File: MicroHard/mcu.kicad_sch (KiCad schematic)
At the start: 1 part, among them U3 efm32gg842f1024

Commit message: MCU schematic
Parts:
- removed U3: efm32gg842f1024, EFM32GG842F1024:QFP64_10X10, symbol EFM32GG842F1024:efm32gg842f1024
- added C45, C50, C54: 10 µ, symbol Device:C_Polarized_US
- added C46, C48, C49, C52: 0.1 µ, symbol Device:C
- added C47: 1 µ, symbol Device:C
- added C51, C53: 10 n, symbol Device:C
- added C55, C56: 12 p, symbol Device:C
- added D1: LED, symbol Device:LED
- added J1: MCU_Debug, Connector_PinHeader_1.00mm:PinHeader_2x10_P1.00mm_Vertical, symbol Connector_Generic:Conn_02x10_Odd_Even
- added J2: Controller Connector, symbol Connector:Conn_01x07_Socket
- added J3: GPIO_header, Connector_JST:JST_XH_B8B-XH-AM_1x08_P2.50mm_Vertical, symbol Connector:Conn_01x08_Pin
- added R11: R, symbol Device:R
- added R12, R13: 10k, Resistor_SMD:R_1206_3216Metric_Pad1.30x1.75mm_HandSolder, symbol Device:R
- added SW1, SW2: KMR221NGLFS, KMR221_CNK, symbol Button:KMR221NGLFS
- added U3: EFM32GG842F1024, EFM32GG842F1024:QFP64_10X10, symbol EFM32GG842F1024:efm32gg842f1024_improved_layout
- added Y1: 48 MHz, symbol Device:Crystal_GND24
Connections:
- new net: J3.1 (Pin_1), U3.13 (PC4)
- new net: J3.2 (Pin_2), U3.14 (PC5)
- new net: C56.1, U3.24 (PB13), Y1.3
- new net: C55.1, U3.25 (PB14), Y1.1
- new net: J3.3 (Pin_3), U3.37 (PC6)
- new net: J3.4 (Pin_4), U3.38 (PC7)
- new net: J3.5 (Pin_5), U3.45 (PC12)
- new net: J3.6 (Pin_6), U3.46 (PC13)
- new net: J3.7 (Pin_7), U3.47 (PC14)
- new net: J3.8 (Pin_8), U3.48 (PC15)
- new net: J1.9 (Pin_9), U3.49 (PF0)
- new net: J1.7 (Pin_7), U3.50 (PF1)
- new net: J1.13 (Pin_13), U3.51 (PF2)
- new net: R11.2, U3.9 (PB3)
- new net: R12.1, SW1.2
- new net: D1.2 (A), R11.1
- new net: C47.1, U3.40 (DECOUPLE)
- new net: R13.2, SW2.1
- new net +3.3V: C45.1, C46.1, C48.1, C49.1, C50.1, C51.1, C52.1, C53.1, C54.1, J1.1 (Pin_1), R13.1, SW1.1, U3.23 (AVDD_1), U3.26 (IOVDD_3), U3.27 (AVDD_0), U3.39 (VDD_DREG), U3.55 (IOVDD_5), U3.7 (IOVDD_0)
- new net +3.3VA: J2.1 (Pin_1)
- new net Btn_1: SW1.3, U3.10 (PB4)
- new net ControllerBtn: J2.6 (Pin_6), U3.31 (PD3)
- new net ControllerX: J2.3 (Pin_3), U3.28 (PD0)
- new net ControllerY: J2.4 (Pin_4), U3.29 (PD1)
- new net ControllerZ: J2.5 (Pin_5), U3.30 (PD2)
- new net FPGA_GPIO0: U3.58 (PE9)
- new net FPGA_GPIO1: U3.57 (PE8)
- new net FPGA_RESET: U3.44 (PE7)
- new net FPGA_US0_CLK: U3.61 (PE12)
- new net FPGA_US0_CS: U3.62 (PE13)
- new net FPGA_US0_RX: U3.60 (PE11)
- new net FPGA_US0_TX: U3.59 (PE10)
- new net GND: C45.2, C46.2, C47.2, C48.2, C49.2, C50.2, C51.2, C52.2, C53.2, C54.2, C55.2, C56.2, D1.1 (K), J1.10 (Pin_10), J1.12 (Pin_12), J1.14 (Pin_14), J1.16 (Pin_16), J1.18 (Pin_18), J1.20 (Pin_20), J1.4 (Pin_4), J1.6 (Pin_6), J1.8 (Pin_8), J2.2 (Pin_2), R12.2, SW2.2, U3.22 (VSS), U3.56 (VSS), U3.8 (VSS), Y1.2, Y1.4
- new net I2C0_SCL: U3.2 (PA1)
- new net I2C0_SDA: U3.1 (PA0)
- new net MCU_Reset: J1.15 (Pin_15), SW2.4, U3.20 (RESETN)
- no-connect marks 0 -> 9
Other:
- title: (none) -> Microcontroller unit

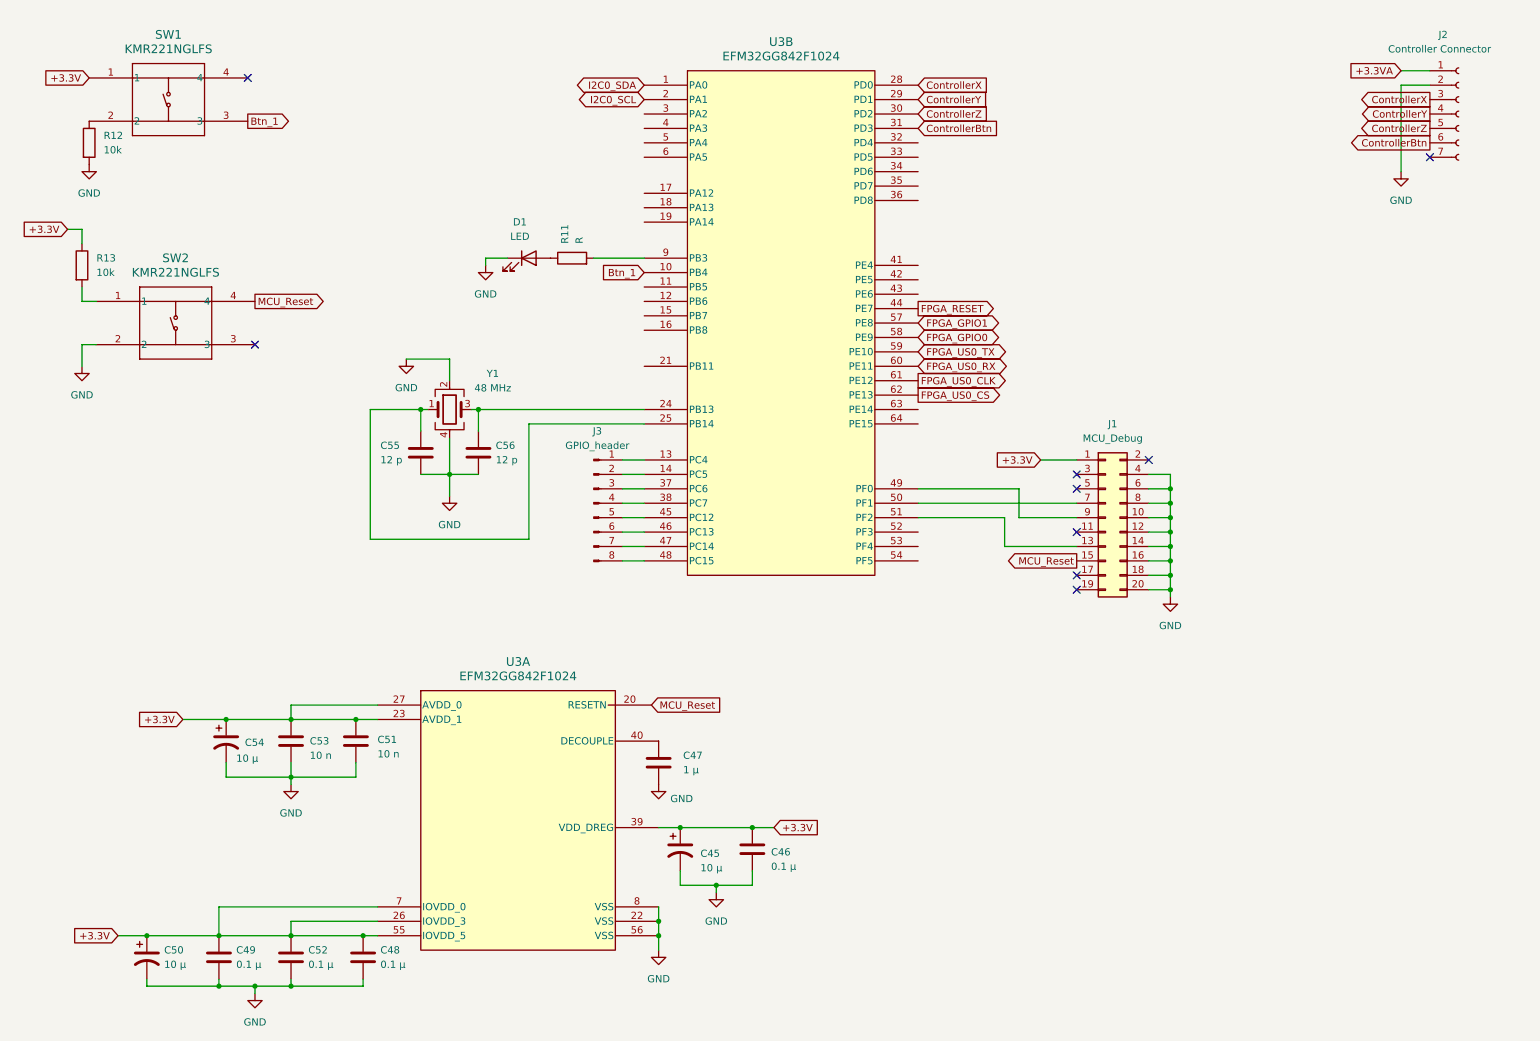
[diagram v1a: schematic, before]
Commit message: feat: VGA out lines from FPGA drawn
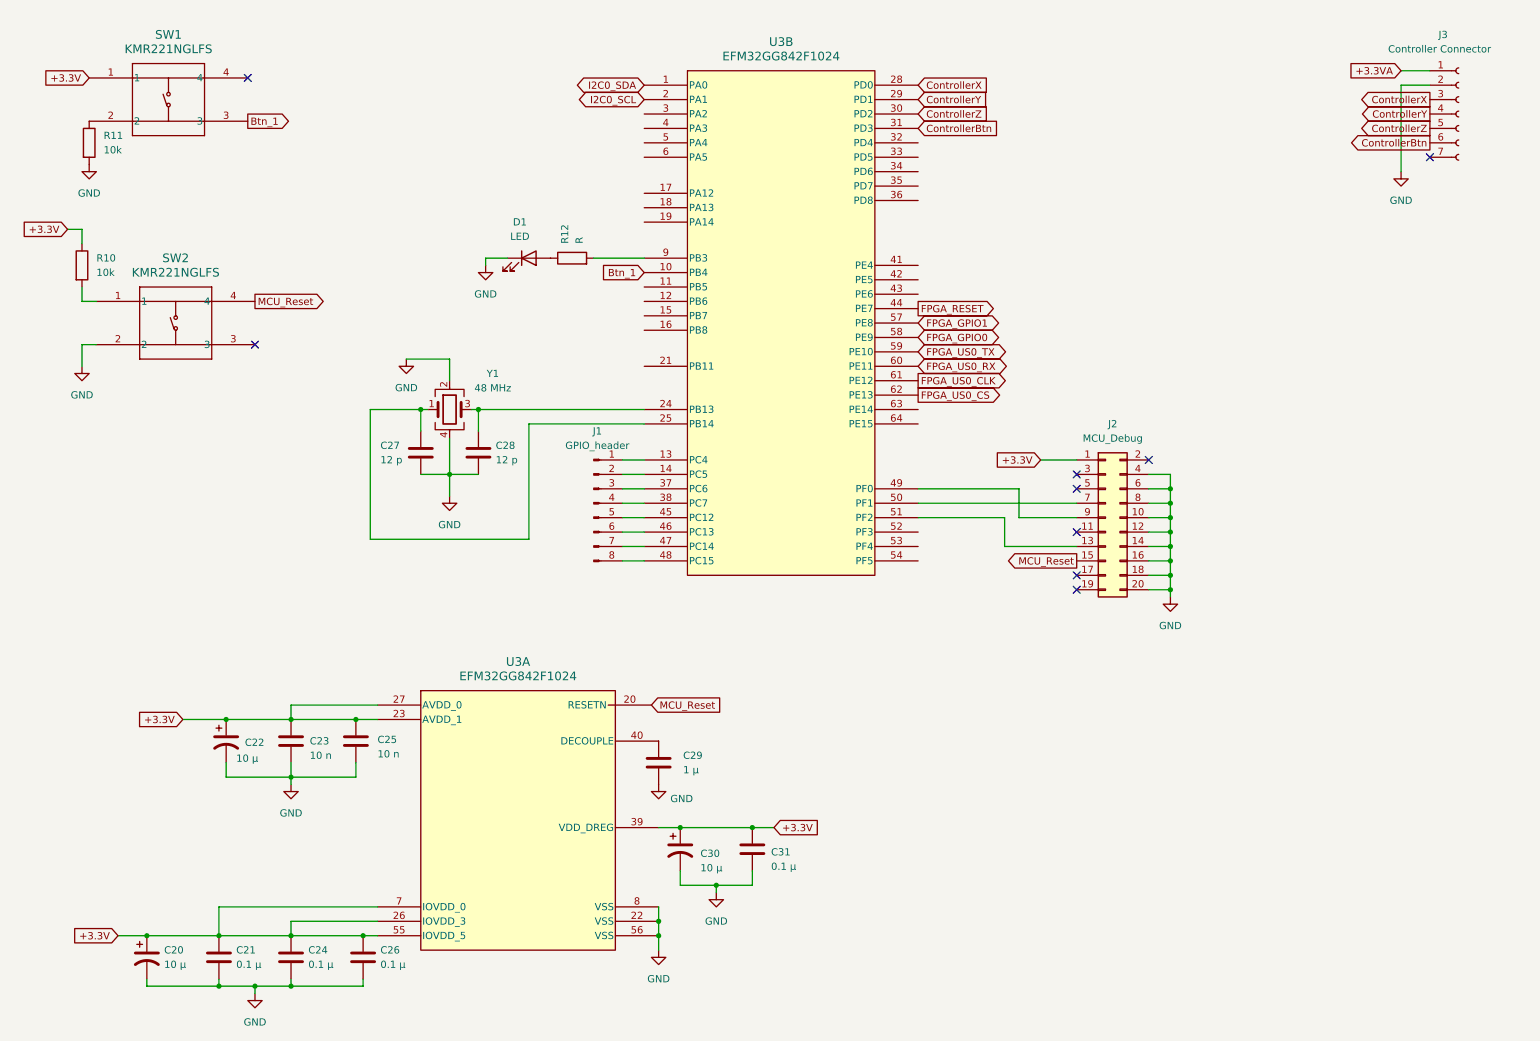
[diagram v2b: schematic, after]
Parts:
- renumbered C50 to C20, C49 to C21, C54 to C22, C53 to C23, C52 to C24, C51 to C25, C48 to C26, C55 to C27, C56 to C28, C47 to C29, C45 to C30, C46 to C31, J3 to J1, J1 to J2, J2 to J3, R13 to R10, R12 to R11, R11 to R12
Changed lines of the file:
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@@
 		(on_board yes)
 		(dnp no)
-		(property "Reference" "C46"
+		(property "Reference" "C31"
 			(at 149.352 164.338 0)
 			(effects
@@
 			(project ""
 				(path "/578bd531-a491-4b15-a479-460d159ffc14/51bb8540-90e7-4b9a-973c-776e3825d084"
-					(reference "C46")
+					(reference "C31")
 					(unit 1)
 				)
@@
 		(on_board yes)
 		(dnp no)
-		(property "Reference" "C52"
+		(property "Reference" "C24"
 			(at 67.818 181.61 0)
 			(effects
@@
 			(project ""
 				(path "/578bd531-a491-4b15-a479-460d159ffc14/51bb8540-90e7-4b9a-973c-776e3825d084"
-					(reference "C52")
+					(reference "C24")
 					(unit 1)
 				)
@@
 		(on_board yes)
 		(dnp no)
-		(property "Reference" "#PWR020"
+		(property "Reference" "#PWR016"
 			(at 129.54 158.75 0)
 			(effects
@@
 			(project ""
 				(path "/578bd531-a491-4b15-a479-460d159ffc14/51bb8540-90e7-4b9a-973c-776e3825d084"
-					(reference "#PWR020")
+					(reference "#PWR016")
 					(unit 1)
 				)
@@
 		(dnp no)
 		(fields_autoplaced yes)
-		(property "Reference" "R12"
+		(property "Reference" "R11"
 			(at 31.75 38.0999 0)
 			(effects
@@
 			(project ""
 				(path "/578bd531-a491-4b15-a479-460d159ffc14/51bb8540-90e7-4b9a-973c-776e3825d084"
-					(reference "R12")
+					(reference "R11")
 					(unit 1)
 				)
@@
 		(dnp no)
 		(fields_autoplaced yes)
-		(property "Reference" "R11"
+		(property "Reference" "R12"
 			(at 113.0299 57.15 0)
 			(effects
@@
 			(project ""
 				(path "/578bd531-a491-4b15-a479-460d159ffc14/51bb8540-90e7-4b9a-973c-776e3825d084"
-					(reference "R11")
+					(reference "R12")
 					(unit 1)
 				)
@@
 		(dnp no)
 		(fields_autoplaced yes)
-		(property "Reference" "#PWR025"
+		(property "Reference" "#PWR013"
 			(at 85.09 83.82 0)
 			(effects
@@
 			(project ""
 				(path "/578bd531-a491-4b15-a479-460d159ffc14/51bb8540-90e7-4b9a-973c-776e3825d084"
-					(reference "#PWR025")
+					(reference "#PWR013")
 					(unit 1)
 				)
@@
 		(on_board yes)
 		(dnp no)
-		(property "Reference" "C53"
+		(property "Reference" "C23"
 			(at 68.072 144.78 0)
 			(effects
@@
 			(project ""
 				(path "/578bd531-a491-4b15-a479-460d159ffc14/51bb8540-90e7-4b9a-973c-776e3825d084"
-					(reference "C53")
+					(reference "C23")
 					(unit 1)
 				)
@@
 		(on_board yes)
 		(dnp no)
-		(property "Reference" "C49"
+		(property "Reference" "C21"
 			(at 55.118 181.61 0)
 			(effects
@@
 			(project ""
 				(path "/578bd531-a491-4b15-a479-460d159ffc14/51bb8540-90e7-4b9a-973c-776e3825d084"
-					(reference "C49")
+					(reference "C21")
 					(unit 1)
 				)
@@
 		(dnp no)
 		(fields_autoplaced yes)
-		(property "Reference" "#PWR027"
+		(property "Reference" "#PWR09"
 			(at 27.94 85.09 0)
 			(effects
@@
 			(project ""
 				(path "/578bd531-a491-4b15-a479-460d159ffc14/51bb8540-90e7-4b9a-973c-776e3825d084"
-					(reference "#PWR027")
+					(reference "#PWR09")
 					(unit 1)
 				)
@@
 		(dnp no)
 		(fields_autoplaced yes)
-		(property "Reference" "#PWR015"
+		(property "Reference" "#PWR020"
 			(at 260.35 50.8 0)
 			(effects
@@
 			(project ""
 				(path "/578bd531-a491-4b15-a479-460d159ffc14/51bb8540-90e7-4b9a-973c-776e3825d084"
-					(reference "#PWR015")
+					(reference "#PWR020")
 					(unit 1)
 				)
@@
 		(on_board yes)
 		(dnp no)
-		(property "Reference" "J2"
+		(property "Reference" "J3"
 			(at 266.954 20.32 0)
 			(effects
@@
 			(project ""
 				(path "/578bd531-a491-4b15-a479-460d159ffc14/51bb8540-90e7-4b9a-973c-776e3825d084"
-					(reference "J2")
+					(reference "J3")
 					(unit 1)
 				)
@@
 		(dnp no)
 		(fields_autoplaced yes)
-		(property "Reference" "J3"
+		(property "Reference" "J1"
 			(at 118.745 90.17 0)
 			(effects
@@
 			(project ""
 				(path "/578bd531-a491-4b15-a479-460d159ffc14/51bb8540-90e7-4b9a-973c-776e3825d084"
-					(reference "J3")
+					(reference "J1")
 					(unit 1)
 				)
@@
 		(on_board yes)
 		(dnp no)
-		(property "Reference" "C50"
+		(property "Reference" "C20"
 			(at 42.418 181.61 0)
 			(effects
@@
 			(project "MicroHard"
 				(path "/578bd531-a491-4b15-a479-460d159ffc14/51bb8540-90e7-4b9a-973c-776e3825d084"
-					(reference "C50")
+					(reference "C20")
 					(unit 1)
 				)
@@
 		(on_board yes)
 		(dnp no)
-		(property "Reference" "C56"
+		(property "Reference" "C28"
 			(at 100.838 92.71 0)
 			(effects
@@
 			(project ""
 				(path "/578bd531-a491-4b15-a479-460d159ffc14/51bb8540-90e7-4b9a-973c-776e3825d084"
-					(reference "C56")
+					(reference "C28")
 					(unit 1)
 				)
@@
 		(dnp no)
 		(fields_autoplaced yes)
-		(property "Reference" "#PWR016"
+		(property "Reference" "#PWR012"
 			(at 64.77 158.75 0)
 			(effects
@@
 			(project ""
 				(path "/578bd531-a491-4b15-a479-460d159ffc14/51bb8540-90e7-4b9a-973c-776e3825d084"
-					(reference "#PWR016")
+					(reference "#PWR012")
 					(unit 1)
 				)
@@
 		(dnp no)
 		(fields_autoplaced yes)
-		(property "Reference" "#PWR024"
+		(property "Reference" "#PWR014"
 			(at 92.71 107.95 0)
 			(effects
@@
 			(project ""
 				(path "/578bd531-a491-4b15-a479-460d159ffc14/51bb8540-90e7-4b9a-973c-776e3825d084"
-					(reference "#PWR024")
+					(reference "#PWR014")
 					(unit 1)
 				)
@@
 		(dnp no)
 		(fields_autoplaced yes)
-		(property "Reference" "#PWR014"
+		(property "Reference" "#PWR018"
 			(at 139.7 177.8 0)
 			(effects
@@
 			(project ""
 				(path "/578bd531-a491-4b15-a479-460d159ffc14/51bb8540-90e7-4b9a-973c-776e3825d084"
-					(reference "#PWR014")
+					(reference "#PWR018")
 					(unit 1)
 				)
@@
 		(on_board yes)
 		(dnp no)
-		(property "Reference" "C51"
+		(property "Reference" "C25"
 			(at 80.01 144.526 0)
 			(effects
@@
 			(project ""
 				(path "/578bd531-a491-4b15-a479-460d159ffc14/51bb8540-90e7-4b9a-973c-776e3825d084"
-					(reference "C51")
+					(reference "C25")
 					(unit 1)
 				)
@@
 		(on_board yes)
 		(dnp no)
-		(property "Reference" "C48"
+		(property "Reference" "C26"
 			(at 80.518 181.61 0)
 			(effects
@@
 			(project ""
 				(path "/578bd531-a491-4b15-a479-460d159ffc14/51bb8540-90e7-4b9a-973c-776e3825d084"
-					(reference "C48")
+					(reference "C26")
 					(unit 1)
 				)
@@
 		(dnp no)
 		(fields_autoplaced yes)
-		(property "Reference" "J1"
+		(property "Reference" "J2"
 			(at 209.55 88.9 0)
 			(effects
@@
 			(project ""
 				(path "/578bd531-a491-4b15-a479-460d159ffc14/51bb8540-90e7-4b9a-973c-776e3825d084"
-					(reference "J1")
+					(reference "J2")
 					(unit 1)
 				)
@@
 		(on_board yes)
 		(dnp no)
-		(property "Reference" "C54"
+		(property "Reference" "C22"
 			(at 56.642 145.034 0)
 			(effects
@@
 			(project ""
 				(path "/578bd531-a491-4b15-a479-460d159ffc14/51bb8540-90e7-4b9a-973c-776e3825d084"
-					(reference "C54")
+					(reference "C22")
 					(unit 1)
 				)
@@
 		(on_board yes)
 		(dnp no)
-		(property "Reference" "C45"
+		(property "Reference" "C30"
 			(at 136.906 164.592 0)
 			(effects
@@
 			(project "MicroHard"
 				(path "/578bd531-a491-4b15-a479-460d159ffc14/51bb8540-90e7-4b9a-973c-776e3825d084"
-					(reference "C45")
+					(reference "C30")
 					(unit 1)
 				)
@@
 		(dnp no)
 		(fields_autoplaced yes)
-		(property "Reference" "#PWR022"
+		(property "Reference" "#PWR015"
 			(at 99.06 67.31 0)
 			(effects
@@
 			(project ""
 				(path "/578bd531-a491-4b15-a479-460d159ffc14/51bb8540-90e7-4b9a-973c-776e3825d084"
-					(reference "#PWR022")
+					(reference "#PWR015")
 					(unit 1)
 				)
@@
 		(dnp no)
 		(fields_autoplaced yes)
-		(property "Reference" "#PWR023"
+		(property "Reference" "#PWR019"
 			(at 219.71 125.73 0)
 			(effects
@@
 			(project ""
 				(path "/578bd531-a491-4b15-a479-460d159ffc14/51bb8540-90e7-4b9a-973c-776e3825d084"
-					(reference "#PWR023")
+					(reference "#PWR019")
 					(unit 1)
 				)
@@
 		(dnp no)
 		(fields_autoplaced yes)
-		(property "Reference" "#PWR017"
+		(property "Reference" "#PWR011"
 			(at 58.42 195.58 0)
 			(effects
@@
 			(project ""
 				(path "/578bd531-a491-4b15-a479-460d159ffc14/51bb8540-90e7-4b9a-973c-776e3825d084"
-					(reference "#PWR017")
+					(reference "#PWR011")
 					(unit 1)
 				)
@@
 		(on_board yes)
 		(dnp no)
-		(property "Reference" "C55"
+		(property "Reference" "C27"
 			(at 80.518 92.71 0)
 			(effects
@@
 			(project ""
 				(path "/578bd531-a491-4b15-a479-460d159ffc14/51bb8540-90e7-4b9a-973c-776e3825d084"
-					(reference "C55")
+					(reference "C27")
 					(unit 1)
 				)
@@
 		(dnp no)
 		(fields_autoplaced yes)
-		(property "Reference" "R13"
+		(property "Reference" "R10"
 			(at 30.48 59.6899 0)
 			(effects
@@
 			(project "MicroHard"
 				(path "/578bd531-a491-4b15-a479-460d159ffc14/51bb8540-90e7-4b9a-973c-776e3825d084"
-					(reference "R13")
+					(reference "R10")
 					(unit 1)
 				)
@@
 		(dnp no)
 		(fields_autoplaced yes)
-		(property "Reference" "#PWR026"
+		(property "Reference" "#PWR010"
 			(at 29.21 49.53 0)
 			(effects
@@
 			(project ""
 				(path "/578bd531-a491-4b15-a479-460d159ffc14/51bb8540-90e7-4b9a-973c-776e3825d084"
-					(reference "#PWR026")
+					(reference "#PWR010")
 					(unit 1)
 				)
@@
 		(dnp no)
 		(fields_autoplaced yes)
-		(property "Reference" "#PWR019"
+		(property "Reference" "#PWR017"
 			(at 129.54 187.96 0)
 			(effects
@@
 			(project ""
 				(path "/578bd531-a491-4b15-a479-460d159ffc14/51bb8540-90e7-4b9a-973c-776e3825d084"
-					(reference "#PWR019")
+					(reference "#PWR017")
 					(unit 1)
 				)
@@
 		(on_board yes)
 		(dnp no)
-		(property "Reference" "C47"
+		(property "Reference" "C29"
 			(at 133.858 147.32 0)
 			(effects
@@
 			(project ""
 				(path "/578bd531-a491-4b15-a479-460d159ffc14/51bb8540-90e7-4b9a-973c-776e3825d084"
-					(reference "C47")
-					(unit 1)
-				)
+					(reference "C29")
+					(unit 1)
+				)

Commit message: Finish display
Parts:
- added D?: LED, LED_SMD:LED_1206_3216Metric_Pad1.42x1.75mm_HandSolder, symbol Device:LED
- added J?: Micro_SD_Card_Det2, Connector_Card:microSD_HC_Hirose_DM3AT-SF-PEJM5, symbol Connector:Micro_SD_Card_Det2
- added R?: 68, Resistor_SMD:R_1206_3216Metric_Pad1.30x1.75mm_HandSolder, symbol Device:R
- added R?: 10k, Resistor_SMD:R_0805_2012Metric_Pad1.20x1.40mm_HandSolder, symbol Device:R
- added SW?: KMR221NGLFS, KMR221_CNK, symbol Button:KMR221NGLFS
- C20, C22, C30: value 10 µ -> 10u
- C21, C24, C26, C31: value 0.1 µ -> 0.1u
- C23, C25: value 10 n -> 10n
- C27, C28: value 12 p -> 30p; footprint (none) -> Capacitor_SMD:C_0805_2012Metric_Pad1.18x1.45mm_HandSolder
- C29: value 1 µ -> 1u
- D1: footprint (none) -> LED_SMD:LED_1206_3216Metric_Pad1.42x1.75mm_HandSolder
- J1: footprint Connector_JST:JST_XH_B8B-XH-AM_1x08_P2.50mm_Vertical -> Connector_PinHeader_2.54mm:PinHeader_1x08_P2.54mm_Vertical
- R10, R11: footprint Resistor_SMD:R_1206_3216Metric_Pad1.30x1.75mm_HandSolder -> Resistor_SMD:R_0805_2012Metric_Pad1.20x1.40mm_HandSolder
- R12: value R -> 68; footprint (none) -> Resistor_SMD:R_1206_3216Metric_Pad1.30x1.75mm_HandSolder
- Y1: value 48 MHz -> 48MHz; footprint (none) -> Crystal:Crystal_SMD_3225-4Pin_3.2x2.5mm_HandSoldering
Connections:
- net +3.3V: now also SW?.1
- net +3.3VA: now also J?.4 (VDD)
- net GND: now also D?.1 (K), J?.11 (SHIELD), J?.6 (VSS), R?.2
- net SD_US2_CLK: now reaches U3.11 (PB5)
- net SD_US2_CLK: now also J?.5 (CLK)
- net SD_US2_CS: now reaches U3.12 (PB6)
- net SD_US2_CS: now also J?.2 (DAT3/CD)
- net at U3.13 (PC4): no longer J1.1 (Pin_1)
- net at U3.14 (PC5): no longer J1.2 (Pin_2)
- net US1_CLK: now reaches U3.15 (PB7)
- net US1_CLK: now also J1.1 (Pin_1)
- net US1_CS: now reaches U3.16 (PB8)
- net US1_CS: now also J1.4 (Pin_4)
- net at U3.3 (PA2): now also R12.2
- net US1_RX: now reaches U3.34 (PD6)
- net US1_RX: now also J1.3 (Pin_3)
- net US1_TX: now reaches U3.35 (PD7)
- net US1_TX: now also J1.2 (Pin_2)
- net at U3.37 (PC6): no longer J1.3 (Pin_3)
- net at U3.38 (PC7): no longer J1.4 (Pin_4)
- net at U3.4 (PA3): now also R?.2
- net FPGA_DONE: now reaches U3.43 (PE6)
- net MCU_Btn_1: now reaches U3.5 (PA4)
- net MCU_Btn_1: now also SW?.3
- net MCU_Btn_2: now reaches U3.6 (PA5)
- net MCU_Btn_2: now also SW1.3
- net SD_US2_TX: now reaches U3.9 (PB3)
- net SD_US2_TX: now also J?.3 (CMD); no longer R12.2
- net Btn_1 renamed SD_US2_RX
- net SD_US2_RX: now also J?.7 (DAT0); no longer SW1.3
- net ControllerBtn renamed Controller_Btn
- net ControllerX renamed Controller_X
- net ControllerY renamed Controller_Y
- net ControllerZ renamed Controller_Z
- new net: D?.2 (A), R?.1
- new net: R?.1, SW?.2
- no-connect marks 9 -> 32
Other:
- moved on the sheet: C27, C28, D1, J1, J3, R10, R11, R12, SW1, SW2, Y1
